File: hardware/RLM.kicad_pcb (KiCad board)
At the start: 2 copper layers, 1 part, among them U6 AP1117-33

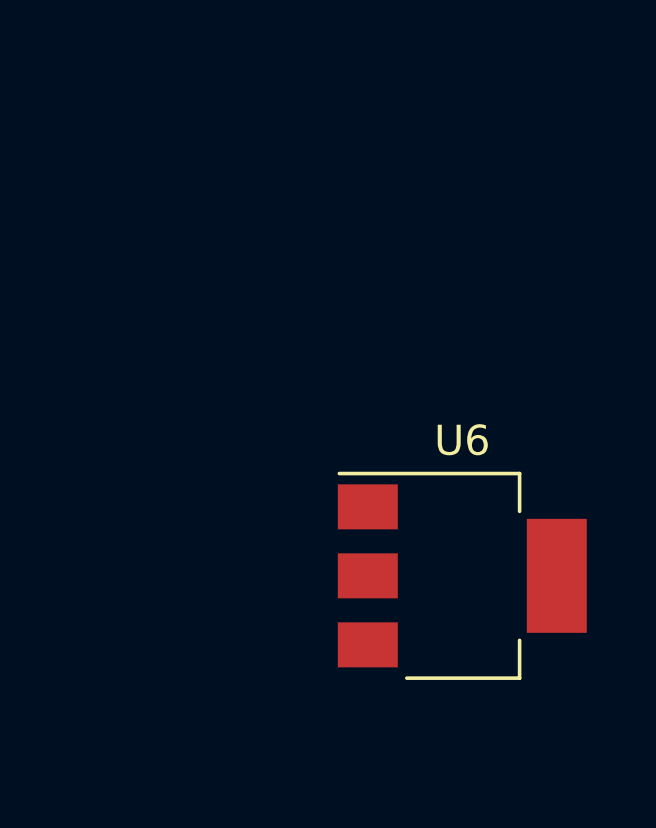
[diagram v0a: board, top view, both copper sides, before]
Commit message: feat: add NRF adapter layout
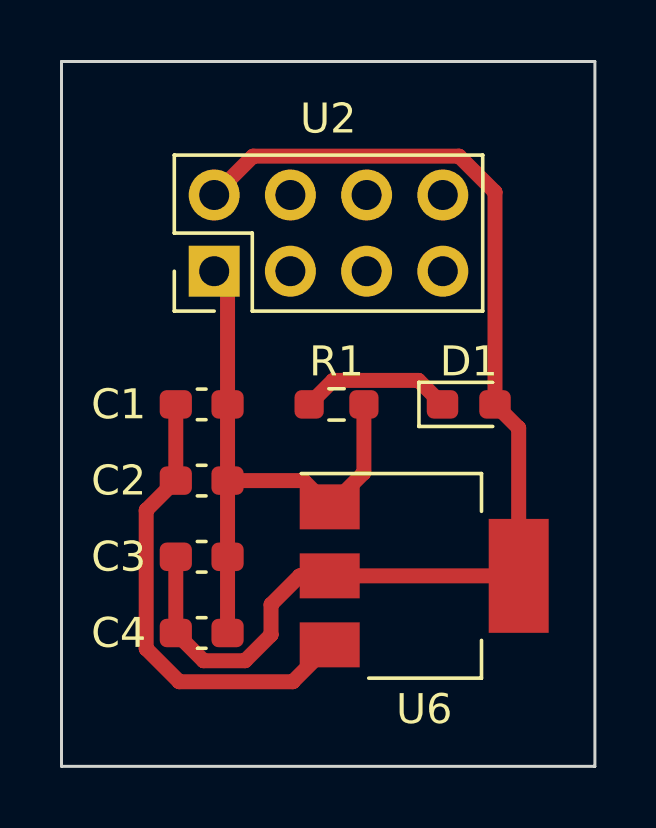
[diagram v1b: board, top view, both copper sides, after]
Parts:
- added C1: 10u, Capacitor_SMD:C_0603_1608Metric_Pad1.08x0.95mm_HandSolder, F.Cu at (138.0, 90.8)
- added C2: 104, Capacitor_SMD:C_0603_1608Metric_Pad1.08x0.95mm_HandSolder, F.Cu at (138.0, 93.3)
- added C3: 10u, Capacitor_SMD:C_0603_1608Metric_Pad1.08x0.95mm_HandSolder, F.Cu at (138.0, 95.9)
- added C4: 104, Capacitor_SMD:C_0603_1608Metric_Pad1.08x0.95mm_HandSolder, F.Cu at (138.0, 98.4)
- added D1: LED, LED_SMD:LED_0603_1608Metric_Pad1.05x0.95mm_HandSolder, F.Cu at (146.9, 90.8)
- added R1: 1k, Resistor_SMD:R_0603_1608Metric_Pad0.98x0.95mm_HandSolder, F.Cu at (142.5, 90.8)
- added U2: ~, Connector_PinHeader_2.54mm:PinHeader_2x04_P2.54mm_Vertical, F.Cu at (138.4, 86.4)
- moved U6 1.27 mm to (145.4, 96.5)
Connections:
- U6 pad 2: GY_VCC -> NRF_VCC
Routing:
- net NRF_VCC: track 0.00 -> 39.6 mm
- net GND: track 0.00 -> 20.5 mm
- net +3.3V: track 0.00 -> 15.6 mm
- net Net-(D1-K): track 0.00 -> 5.11 mm
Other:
- board outline added: 17.8 x 23.5 mm

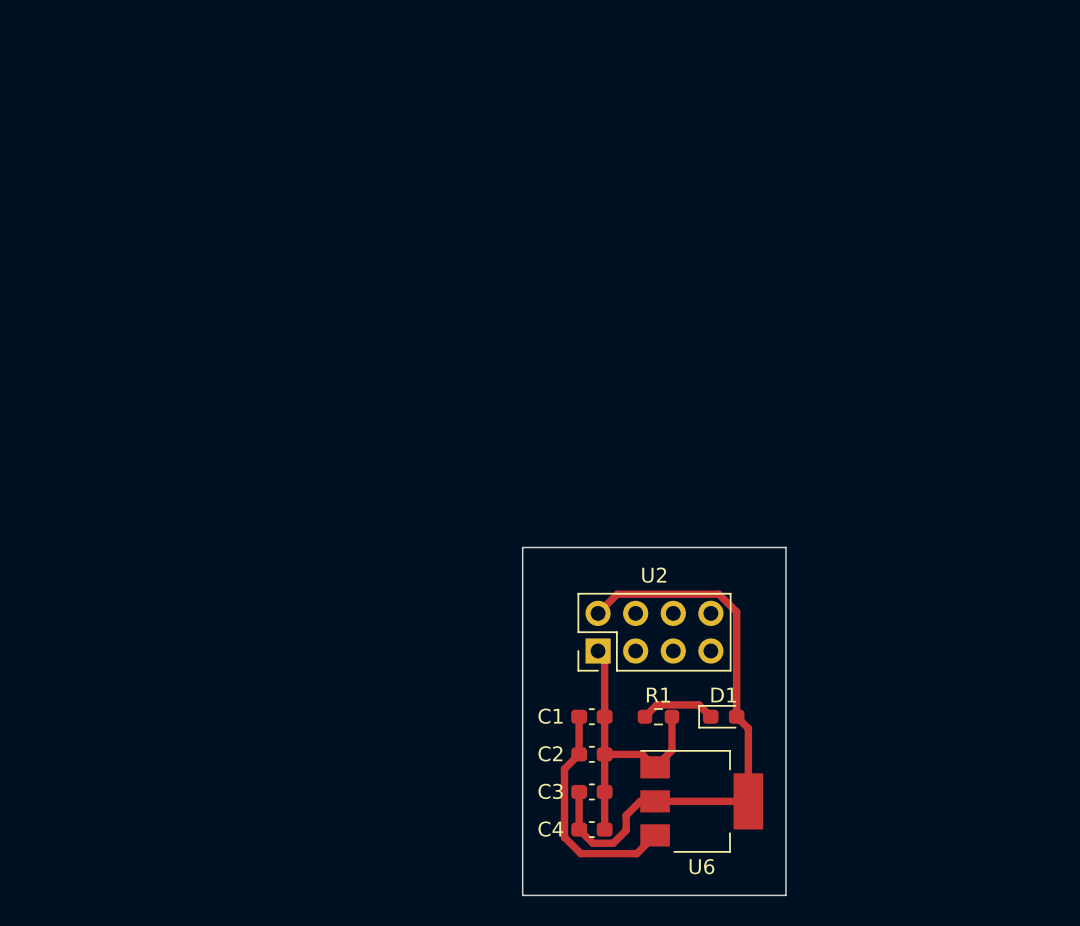
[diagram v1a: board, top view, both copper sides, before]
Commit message: feat: add ESP32, NRF, GY footprints
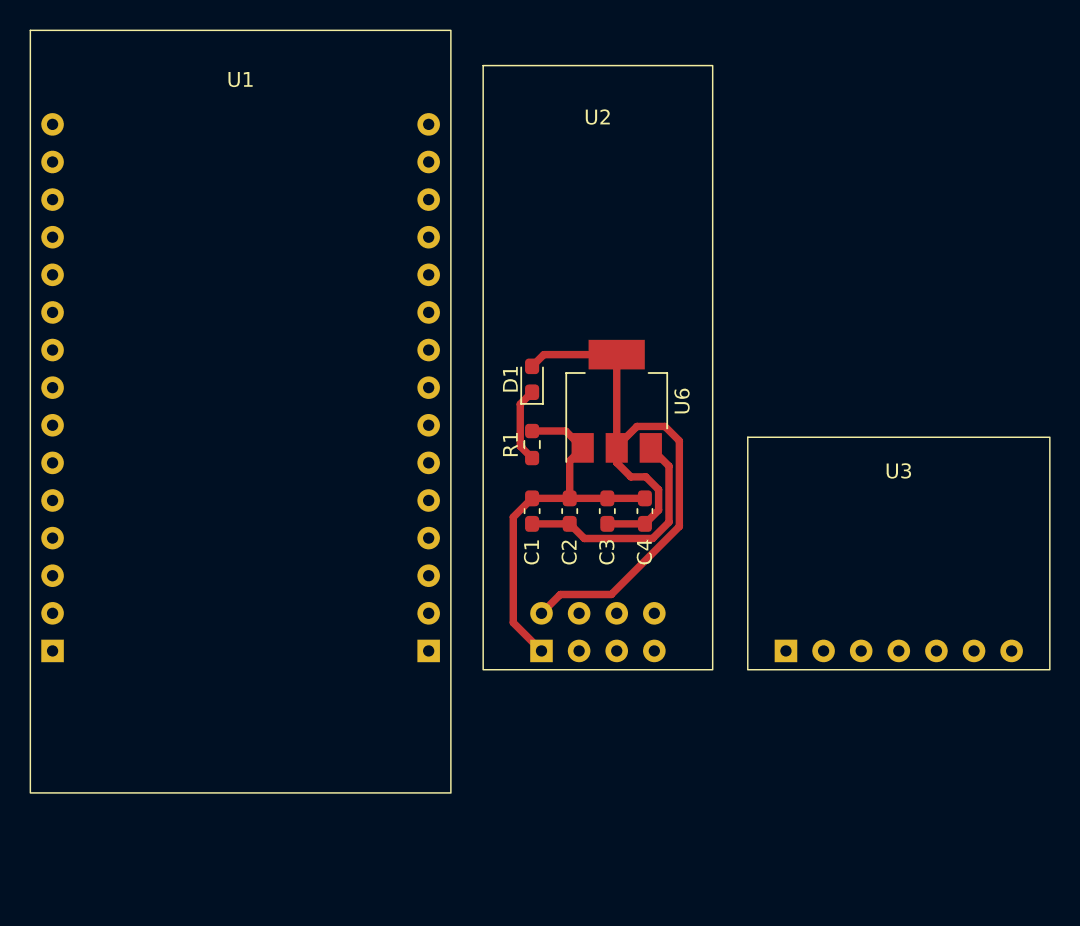
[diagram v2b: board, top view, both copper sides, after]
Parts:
- added U1: ~, GRC:ESP32, F.Cu at (114.3, 44.5)
- added U3: ~, GRC:GY-521, F.Cu at (158.8, 71.9)
- U2: footprint Connector_PinHeader_2.54mm:PinHeader_2x04_P2.54mm_Vertical -> GRC:NRF24L01
- moved U6 27.6 mm to (139.7, 69.5), turned to 90 degrees
- moved D1 26.2 mm to (134.0, 68.0), turned to 90 degrees
- moved C4 21.8 mm to (141.6, 76.9), turned to 90 degrees
- moved R1 20.3 mm to (134.0, 72.4), turned to 90 degrees
- moved C3 19.0 mm to (139.1, 76.9), turned to 90 degrees
- moved C2 16.5 mm to (136.5, 76.9), turned to 90 degrees
- moved C1 14.5 mm to (134.0, 76.9), turned to 90 degrees
- moved U2 1.27 mm to (138.4, 87.6), turned to 0 degrees
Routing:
- net GND: track 20.5 -> 26.9 mm
- net NRF_VCC: track 39.6 -> 45.0 mm
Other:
- board outline removed

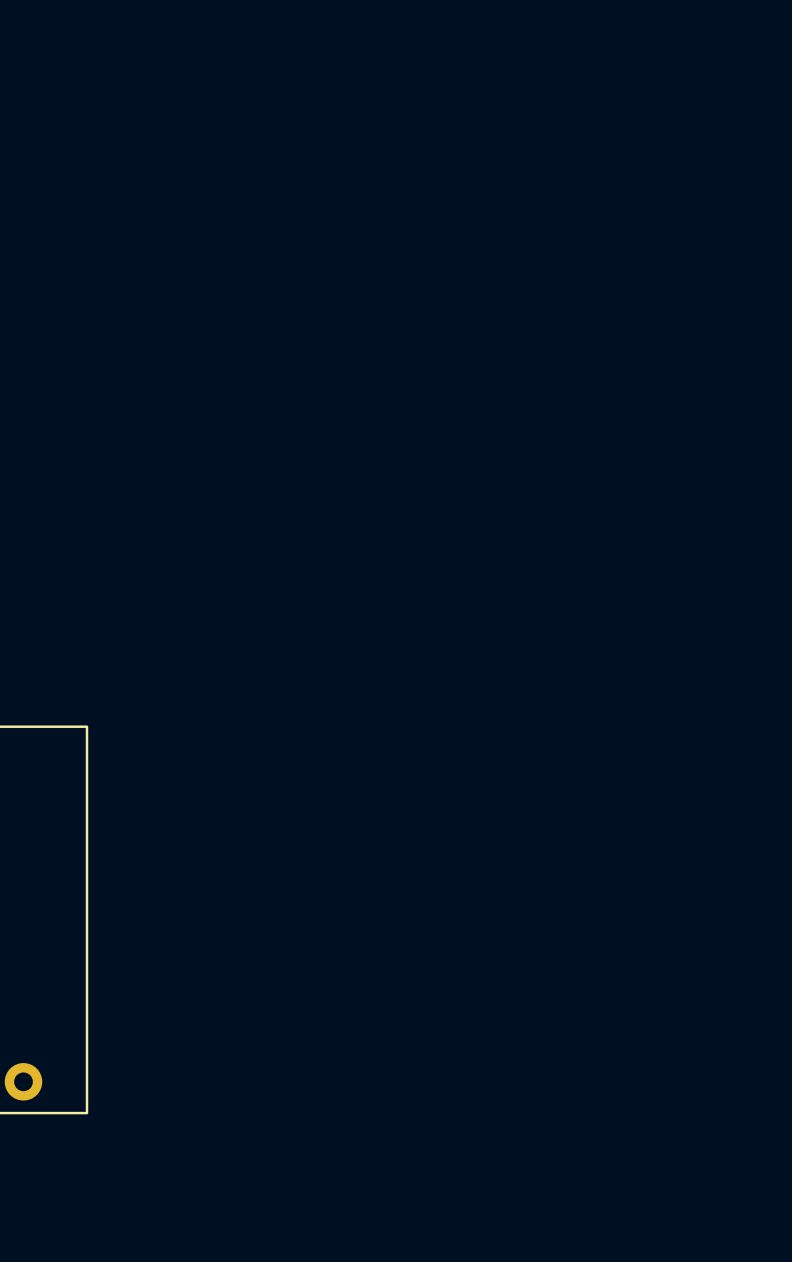
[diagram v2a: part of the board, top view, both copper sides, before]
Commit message: feat: add GY-521 footprint
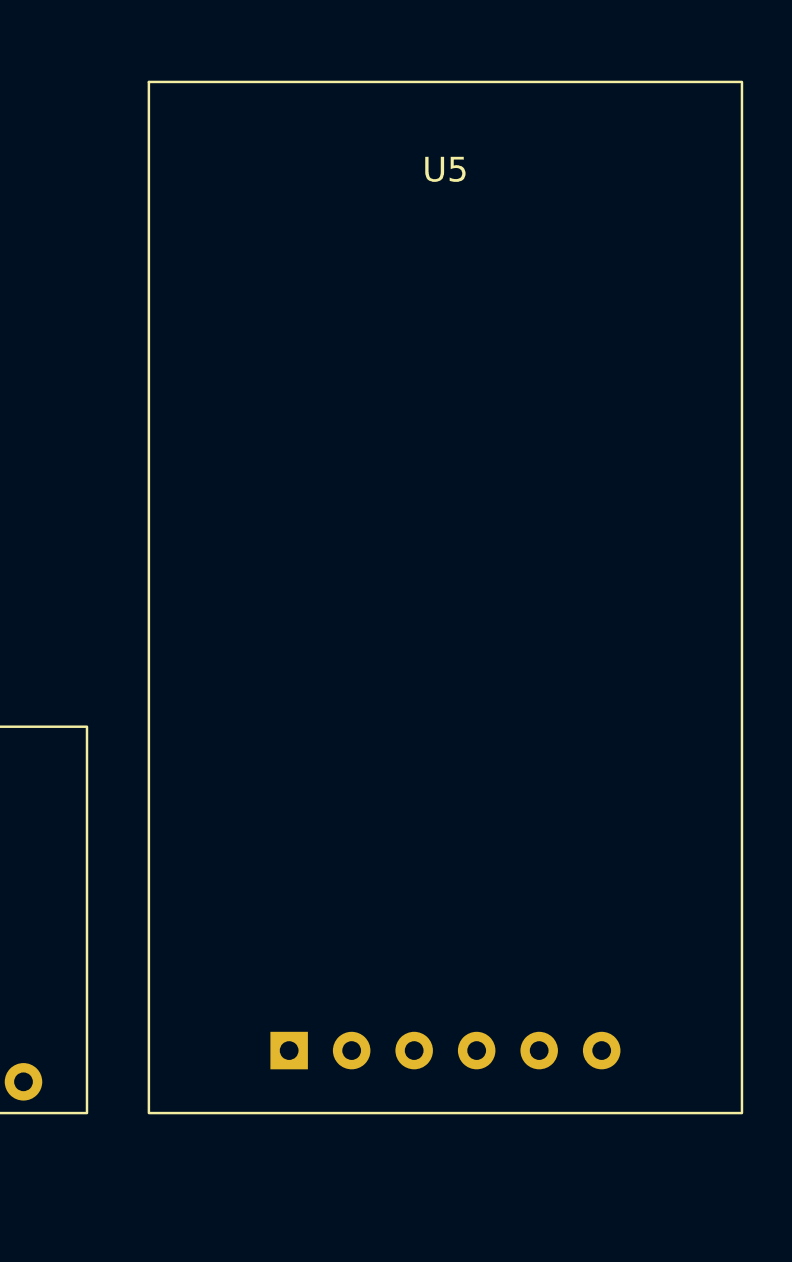
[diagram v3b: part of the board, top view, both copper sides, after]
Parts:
- added U5: ~, GRC:MicroSD-Module, F.Cu at (183.5, 45.7)
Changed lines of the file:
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@@
   (net 34 "unconnected-(U3-XCL-Pad6)")
   (net 35 "unconnected-(U3-ADO-Pad7)")
+  (net 36 "SD_MISO")
+  (net 37 "SD_MOSI")
+  (net 38 "SD_CLK")
+  (net 39 "SD_CS")
+  (footprint "GRC:MicroSD-Module" (layer "F.Cu")
+    (at 183.515 45.73)
+    (property "Sheetfile" "RLM.kicad_sch")
+    (property "Sheetname" "")
+    (attr through_hole)
+    (fp_text reference "U5" (at 0 3.58 unlocked) (layer "F.SilkS")
+        (effects (font (size 1 1) (thickness 0.1)))
+    )
+    (fp_text value "~" (at 0 5.08 unlocked) (layer "F.Fab")
+        (effects (font (size 1 1) (thickness 0.15)))
+    )
+    (fp_text user "${REFERENCE}" (at 0 6.58 unlocked) (layer "F.Fab")
+        (effects (font (size 1 1) (thickness 0.15)))
+    )
+    (fp_rect (start -12.05 0) (end 12.05 41.9)
+      (stroke (width 0.1) (type default)) (fill none) (layer "F.SilkS"))
+    (pad "1" thru_hole rect (at -6.35 39.36) (size 1.524 1.524) (drill 0.762) (layers "*.Cu" "*.Mask")
+      (net 1 "GND") (pinfunction "GND") (pintype "bidirectional"))
+    (pad "2" thru_hole circle (at -3.81 39.36) (size 1.524 1.524) (drill 0.762) (layers "*.Cu" "*.Mask")
+      (net 3 "+3.3V") (pinfunction "VCC") (pintype "bidirectional"))
+    (pad "3" thru_hole circle (at -1.27 39.36) (size 1.524 1.524) (drill 0.762) (layers "*.Cu" "*.Mask")
+      (net 36 "SD_MISO") (pinfunction "MISO") (pintype "bidirectional"))
+    (pad "4" thru_hole circle (at 1.27 39.36) (size 1.524 1.524) (drill 0.762) (layers "*.Cu" "*.Mask")
+      (net 37 "SD_MOSI") (pinfunction "MOSI") (pintype "bidirectional"))
+    (pad "5" thru_hole circle (at 3.81 39.36) (size 1.524 1.524) (drill 0.762) (layers "*.Cu" "*.Mask")
+      (net 38 "SD_CLK") (pinfunction "CLK") (pintype "bidirectional"))
+    (pad "6" thru_hole circle (at 6.35 39.36) (size 1.524 1.524) (drill 0.762) (layers "*.Cu" "*.Mask")
+      (net 39 "SD_CS") (pinfunction "CS") (pintype "bidirectional"))
+  )
   (footprint "GRC:ESP32" (layer "F.Cu")
     (at 114.3 44.45)

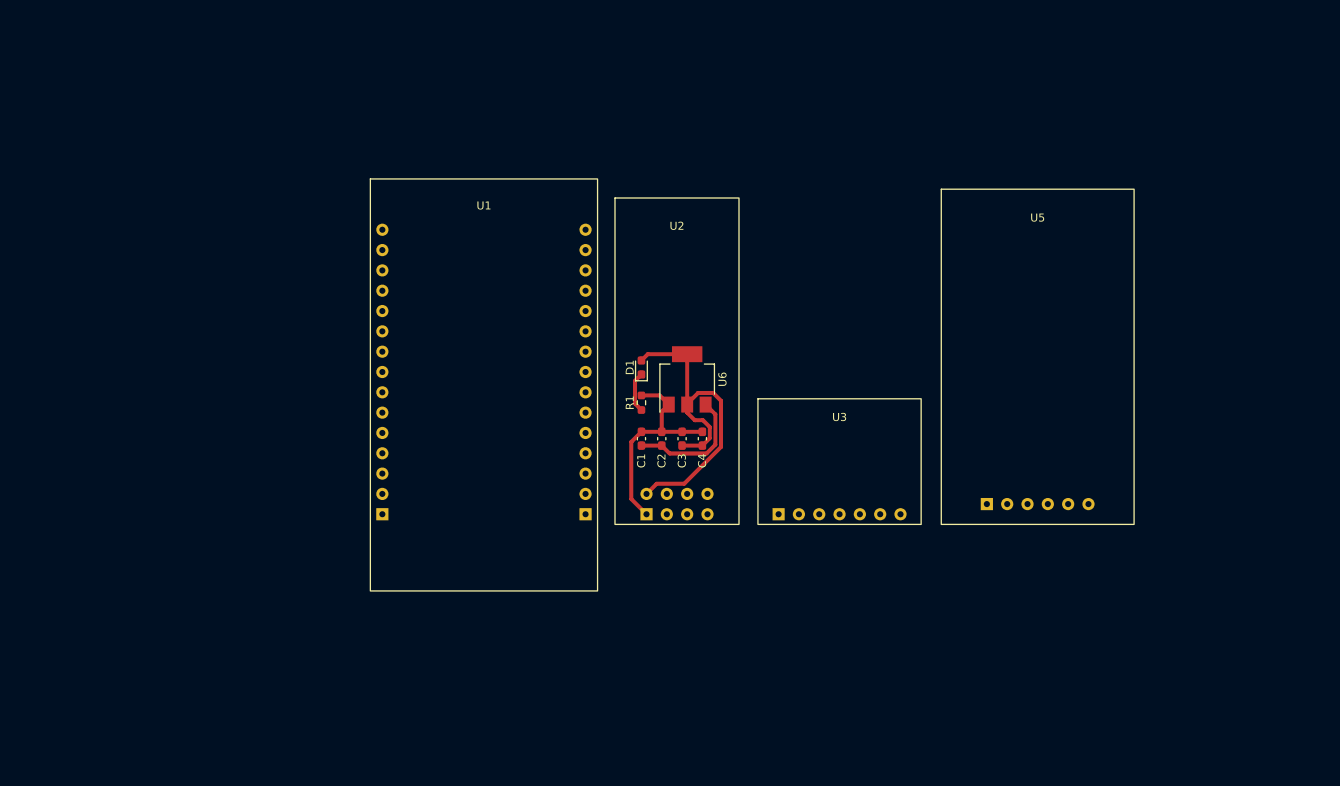
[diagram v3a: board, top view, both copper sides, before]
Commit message: feat: add mounting holes
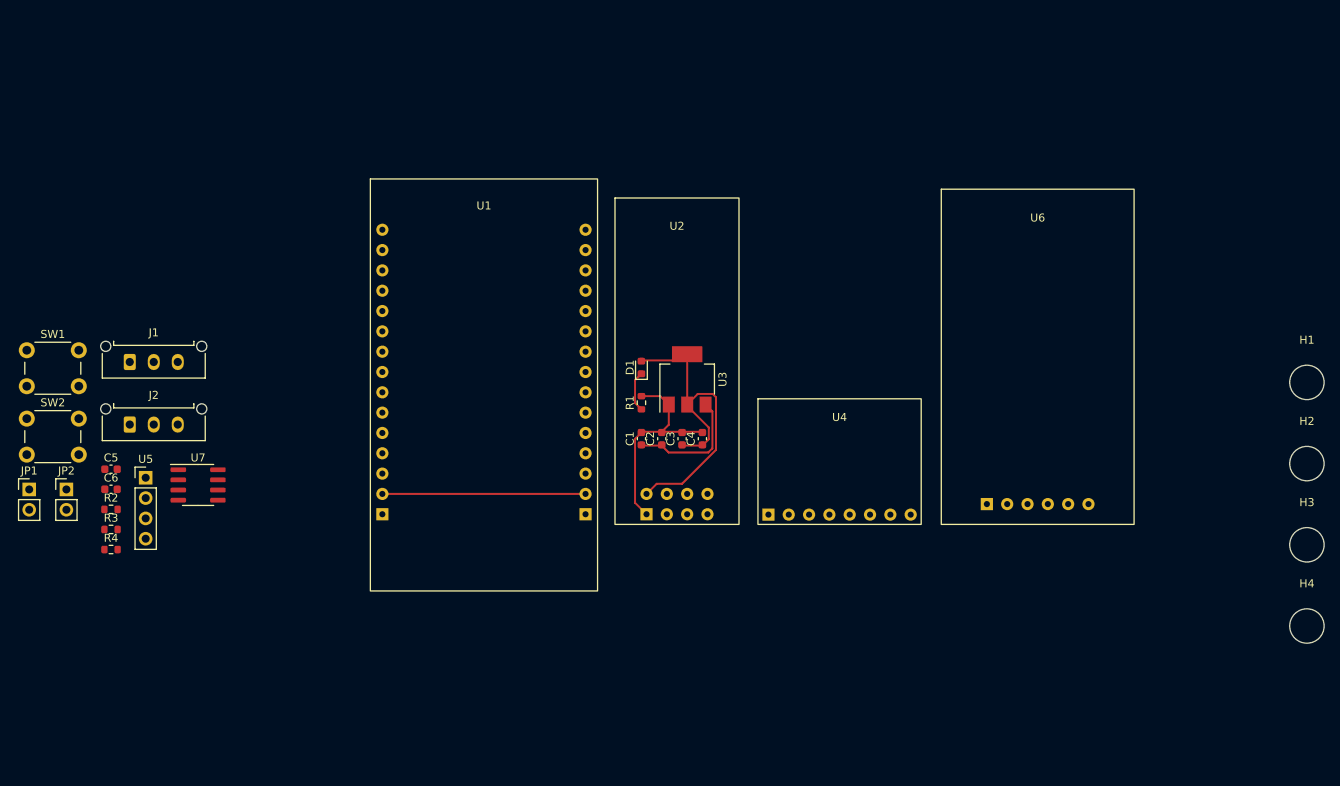
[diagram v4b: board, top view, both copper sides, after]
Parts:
- added C5: 100nF, Capacitor_SMD:C_0603_1608Metric, F.Cu at (67.7, 80.7)
- added C6: 100nF, Capacitor_SMD:C_0603_1608Metric, F.Cu at (67.7, 83.2)
- added H1: MountingHole, MountingHole:MountingHole_4.3mm_M4, F.Cu at (217.2, 69.9)
- added H2: MountingHole, MountingHole:MountingHole_4.3mm_M4, F.Cu at (217.2, 80.0)
- added H3: MountingHole, MountingHole:MountingHole_4.3mm_M4, F.Cu at (217.2, 90.2)
- added H4: MountingHole, MountingHole:MountingHole_4.3mm_M4, F.Cu at (217.2, 100.3)
- added J1: Conn_01x03, Connector_Molex:Molex_Micro-Fit_3.0_43650-0315_1x03_P3.00mm_Vertical, F.Cu at (70.0, 67.3)
- added J2: Conn_01x03, Connector_Molex:Molex_Micro-Fit_3.0_43650-0315_1x03_P3.00mm_Vertical, F.Cu at (70.0, 75.2)
- added JP1: Termination, Connector_PinHeader_2.54mm:PinHeader_1x02_P2.54mm_Vertical, F.Cu at (57.5, 83.3)
- added JP2: Shielding, Connector_PinHeader_2.54mm:PinHeader_1x02_P2.54mm_Vertical, F.Cu at (62.1, 83.3)
- added R2: 120, Resistor_SMD:R_0603_1608Metric, F.Cu at (67.7, 85.8)
- added R3: 10k, Resistor_SMD:R_0603_1608Metric, F.Cu at (67.7, 88.3)
- added R4: 10k, Resistor_SMD:R_0603_1608Metric, F.Cu at (67.7, 90.8)
- added SW1: SW_Push, Button_Switch_THT:SW_PUSH_6mm, F.Cu at (57.2, 65.9)
- added SW2: SW_Push, Button_Switch_THT:SW_PUSH_6mm, F.Cu at (57.2, 74.4)
- added U5: ~, Connector_PinHeader_2.54mm:PinHeader_1x04_P2.54mm_Vertical, F.Cu at (72.0, 81.8)
- added U7: MCP2562-E-SN, Package_SO:SOIC-8_3.9x4.9mm_P1.27mm, F.Cu at (78.6, 82.7)
- C1, C2, C3, C4: footprint Capacitor_SMD:C_0603_1608Metric_Pad1.08x0.95mm_HandSolder -> Capacitor_SMD:C_0603_1608Metric
- D1: footprint LED_SMD:LED_0603_1608Metric_Pad1.05x0.95mm_HandSolder -> LED_SMD:LED_0603_1608Metric
- R1: footprint Resistor_SMD:R_0603_1608Metric_Pad0.98x0.95mm_HandSolder -> Resistor_SMD:R_0603_1608Metric
- renumbered U6 to U3, U3 to U4, U5 to U6
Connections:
- net GY_SCL renamed I2C_SCL
- net GY_SDA renamed I2C_SDA
- U1 pad 10: unconnected-(U1-D27-Pad10) -> SD_CS
- U1 pad 12: unconnected-(U1-D12-Pad12) -> SD_OFF
- U1 pad 13: unconnected-(U1-D13-Pad13) -> MPU_CAL
- U1 pad 18: unconnected-(U1-D15-Pad18) -> V_SENSE
- U1 pad 20: NRF_CE -> unconnected-(U1-D4-Pad20)
- U1 pad 21: BN_TX -> CAN_TX
- U1 pad 22: BN_RX -> CAN_RX
- U1 pad 23: NRF_CSN -> unconnected-(U1-D5-Pad23)
- U1 pad 24: NRF_SCK -> SPI_SCK
- U1 pad 25: NRF_MISO -> SPI_MISO
- U1 pad 30: NRF_MOSI -> SPI_MOSI
- U1 pad 6: unconnected-(U1-D32-Pad6) -> GPS_TX
- U1 pad 7: unconnected-(U1-D33-Pad7) -> GPS_RX
- U1 pad 8: unconnected-(U1-D25-Pad8) -> NRF_CE
- U1 pad 9: unconnected-(U1-D26-Pad9) -> NRF_CSN
- U2 pad 5: NRF_SCK -> SPI_SCK
- U2 pad 6: NRF_MOSI -> SPI_MOSI
- U2 pad 7: NRF_MISO -> SPI_MISO
- U6 pad 2: +3.3V -> +5V
- U6 pad 3: SD_MISO -> SPI_MISO
- U6 pad 4: SD_MOSI -> SPI_MOSI
- U6 pad 5: SD_CLK -> SPI_SCK
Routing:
- net GND: track 26.9 -> 51.8 mm
- net NRF_VCC: track 45.0 -> 43.3 mm

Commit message: feat: initial layout
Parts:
- MicroSD Module: renamed from U6
- moved H4 135.2 mm to (102.2, 29.2), turned to 180 degrees
- moved H2 114.9 mm to (102.2, 80.0), turned to 180 degrees
- moved Shield 91.6 mm to (153.7, 81.3), turned to 180 degrees
- moved Term 91.2 mm to (148.6, 81.3), turned to 180 degrees
- moved BN-220 80.0 mm to (129.8, 26.4)
- moved H3 76.2 mm to (171.4, 29.2), turned to 180 degrees
- moved MicroSD Module 74.9 mm to (119.4, 84.5), turned to 180 degrees
- moved C1 69.9 mm to (76.4, 116.5)
- moved C2 69.9 mm to (78.9, 116.5)
- moved D1 69.9 mm to (76.4, 107.6)
- moved R1 69.9 mm to (76.4, 112.0)
- moved C3 69.9 mm to (81.4, 116.5)
- moved C4 69.9 mm to (84.0, 116.5)
- moved U3 69.9 mm to (82.1, 109.0)
- moved CAN 65.8 mm to (135.6, 80.6)
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- renumbered U5 to BN-220, J2 to CAN, J1 to Dash, U1 to ESP32, U4 to GY-521, SW2 to MPU_CAL, U2 to NRF24L01, SW1 to SD_OFF, JP2 to Shield, JP1 to Term
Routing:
- net GND: track 51.8 -> 16.4 mm
- net NRF_VCC: track 43.3 -> 21.5 mm
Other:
- board outline added: 79.4 x 61 mm
- board text added: "GRC RLM V1 By: Evan R."
